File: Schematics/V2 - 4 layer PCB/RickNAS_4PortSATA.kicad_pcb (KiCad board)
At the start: 4 copper layers, 136.1 x 56.4 mm, 38 parts, among them J1 2227595-1, J10 10076579-002C-TRLF, J2 Conn_01x03, J3 Conn_01x03, J6 POWER, J7 10076579-002C-TRLF, J8 10076579-002C-TRLF, J9 10076579-002C-TRLF, U1 CH32V003FxPx, U2 TLV1117-33

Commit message: Re-added traces
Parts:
- moved R1 42.3 mm to (164.2, 70.6)
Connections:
- J10 pad S2: /RX3+ -> /RX2+
- J10 pad S3: /RX3- -> /RX2-
- J10 pad S5: /TX3- -> /TX2-
- J10 pad S6: /TX3+ -> /TX2+
- J9 pad S2: /RX2+ -> /RX3+
- J9 pad S3: /RX2- -> /RX3-
- J9 pad S5: /TX2- -> /TX3-
- J9 pad S6: /TX2+ -> /TX3+
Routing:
- net /TX2+: track 0.00 -> 54.4 mm, vias 0 -> 1
- net /TX0-: track 0.00 -> 53.2 mm, vias 0 -> 1
- net /TX2-: track 0.00 -> 51.7 mm, vias 0 -> 1
- net /TX0+: track 0.00 -> 51.3 mm, vias 0 -> 1
- net /RX2-: track 0.00 -> 50.1 mm
- net /RX2+: track 0.00 -> 49.8 mm
- net /RX0+: track 0.00 -> 48.0 mm
- net /RX0-: track 0.00 -> 47.7 mm
- net /TX1-: track 0.00 -> 25.1 mm, vias 0 -> 1
- net /TX1+: track 0.00 -> 21.8 mm, vias 0 -> 1
- net /TX3+: track 0.00 -> 21.8 mm, vias 0 -> 1
- net /TX3-: track 0.00 -> 19.8 mm, vias 0 -> 1
- net /RX3-: track 0.00 -> 18.3 mm
- net /RX3+: track 0.00 -> 17.4 mm
- net /RX1+: track 0.00 -> 16.7 mm
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
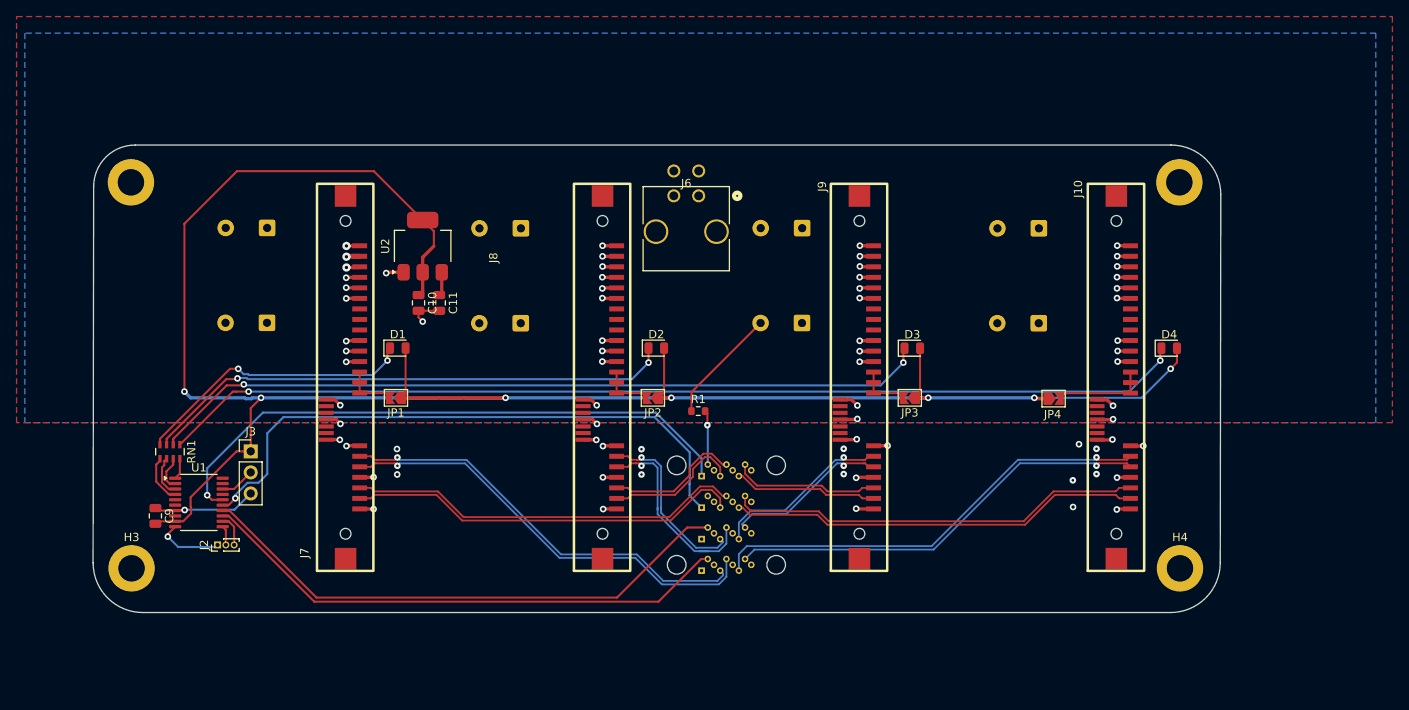
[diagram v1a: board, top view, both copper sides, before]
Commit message: Improved traces and cleaned silkscreen
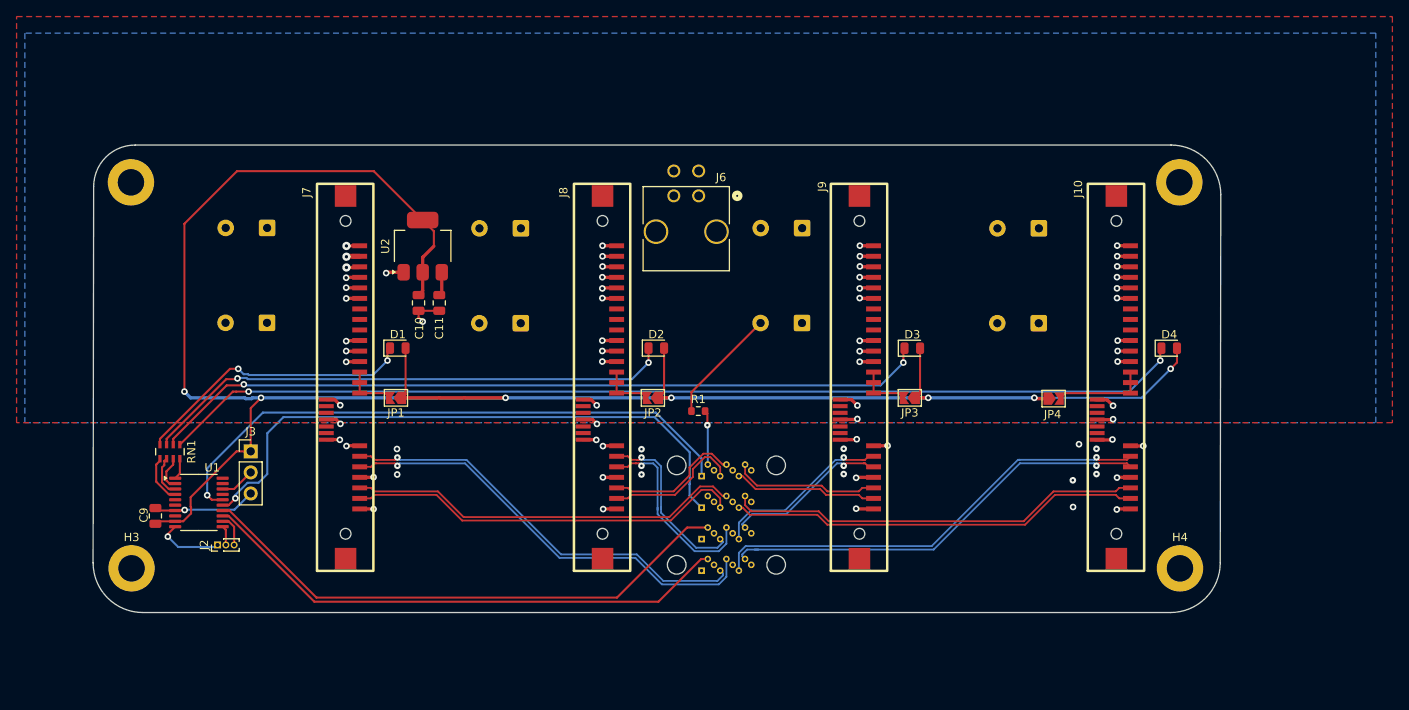
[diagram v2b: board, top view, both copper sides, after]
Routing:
- net /TX2-: track 51.7 -> 53.0 mm
- net /TX1-: track 25.1 -> 24.0 mm
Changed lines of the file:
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@@
 		(tags "capacitor")
 		(property "Reference" "C11"
-			(at 0 -1.68 90)
+			(at 3.05 0 90)
 			(layer "F.SilkS")
 			(effects
@@
 		(tags "TSSOP SO")
 		(property "Reference" "U1"
-			(at 0 -4.2 0)
+			(at 1.6 -4.2 0)
 			(layer "F.SilkS")
 			(effects
@@
 		(at 152.7 47.655 90)
 		(property "Reference" "J8"
-			(at -4.45 -13.15 90)
+			(at 3.455 -4.7 90)
 			(unlocked yes)
 			(layer "F.SilkS")
@@
 		(tags "430450423 ")
 		(property "Reference" "J6"
-			(at -1.5 -1.5 0)
+			(at 2.700001 -2.229998 0)
 			(unlocked yes)
 			(layer "F.SilkS")
@@
 		(tags "capacitor")
 		(property "Reference" "C10"
-			(at 0 -1.68 90)
+			(at 3.05 -0.1 90)
 			(layer "F.SilkS")
 			(effects
@@
 		(at 121.7 47.655 90)
 		(property "Reference" "J7"
-			(at -40.065 -4.95 90)
+			(at 3.455 -4.7 90)
 			(unlocked yes)
 			(layer "F.SilkS")
@@
 		(tags "capacitor")
 		(property "Reference" "C9"
-			(at 0 -1.68 90)
+			(at -0.1 1.4 90)
 			(layer "F.SilkS")
 			(effects
@@
 	)
 	(segment
+		(start 170.136612 87.3091)
+		(end 171.5 87.3091)
+		(width 0.2182)
+		(layer "B.Cu")
+		(net "/TX2-")
+	)
+	(segment
 		(start 212.009101 76.899101)
 		(end 203.062277 76.899101)
@@
 	)
 	(segment
+		(start 169.568201 87.877511)
+		(end 170.136612 87.3091)
+		(width 0.2182)
+		(locked yes)
+		(layer "B.Cu")
+		(net "/TX2-")
+	)
+	(segment
+		(start 169.9 88.45)
+		(end 169.568201 88.118201)
+		(width 0.2182)
+		(layer "B.Cu")
+		(net "/TX2-")
+	)
+	(segment
 		(start 203.062277 76.899101)
 		(end 192.652278 87.3091)
@@
 	)
 	(segment
-		(start 171.0409 87.3091)
-		(end 169.9 88.45)
+		(start 212.3 77.19)
+		(end 212.009101 76.899101)
 		(width 0.2182)
 		(layer "B.Cu")
@@
 	)
 	(segment
-		(start 212.3 77.19)
-		(end 212.009101 76.899101)
+		(start 169.568201 88.118201)
+		(end 169.568201 87.877511)
 		(width 0.2182)
 		(layer "B.Cu")
@@
 	)
 	(segment
-		(start 169.15 89.85)
-		(end 169.15 87.854288)
+		(start 192.413388 86.8909)
+		(end 169.963388 86.8909)
 		(width 0.2182)
 		(layer "B.Cu")
@@
 	)
 	(segment
-		(start 212.009101 76.480899)
-		(end 203.003389 76.480899)
+		(start 202.827144 76.477144)
+		(end 192.413388 86.8909)
 		(width 0.2182)
 		(layer "B.Cu")
@@
 	)
 	(segment
-		(start 203.003389 76.480899)
-		(end 202.999634 76.477144)
+		(start 169.15 87.704288)
+		(end 169.15 89.85)
 		(width 0.2182)
 		(layer "B.Cu")
@@
 	)
 	(segment
-		(start 170.113388 86.8909)
-		(end 192.413388 86.8909)
+		(start 203.003389 76.480899)
+		(end 202.999634 76.477144)
 		(width 0.2182)
 		(layer "B.Cu")
@@
 	)
 	(segment
-		(start 192.413388 86.8909)
-		(end 202.827144 76.477144)
+		(start 212.3 76.19)
+		(end 212.009101 76.480899)
 		(width 0.2182)
 		(layer "B.Cu")
@@
 	)
 	(segment
-		(start 169.15 87.854288)
-		(end 170.113388 86.8909)
+		(start 169.963388 86.8909)
+		(end 169.15 87.704288)
 		(width 0.2182)
 		(layer "B.Cu")
@@
 	)
 	(segment
-		(start 202.999634 76.477144)
-		(end 202.827144 76.477144)
+		(start 212.009101 76.480899)
+		(end 203.003389 76.480899)
 		(width 0.2182)
 		(layer "B.Cu")
@@
 	)
 	(segment
-		(start 212.3 76.19)
-		(end 212.009101 76.480899)
+		(start 202.999634 76.477144)
+		(end 202.827144 76.477144)
 		(width 0.2182)
 		(layer "B.Cu")
@@
 		(width 0.2182)
 		(layer "B.Cu")
-		(net "/TX1-")
-	)
-	(segment
-		(start 165.5 87.51108)
-		(end 164.312568 87.51108)
-		(width 0.2182)
-		(layer "B.Cu")
